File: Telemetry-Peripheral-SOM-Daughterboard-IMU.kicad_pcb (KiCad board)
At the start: 2 copper layers, 32 x 50 mm, 34 parts, among them IC1 FS3000-1015, J1 Conn_02x10_Odd_Even, J2 Conn_01x03_Pin, J3 Conn_01x03_Pin, J4 Conn_01x03_Pin, U1 LSM6DSV

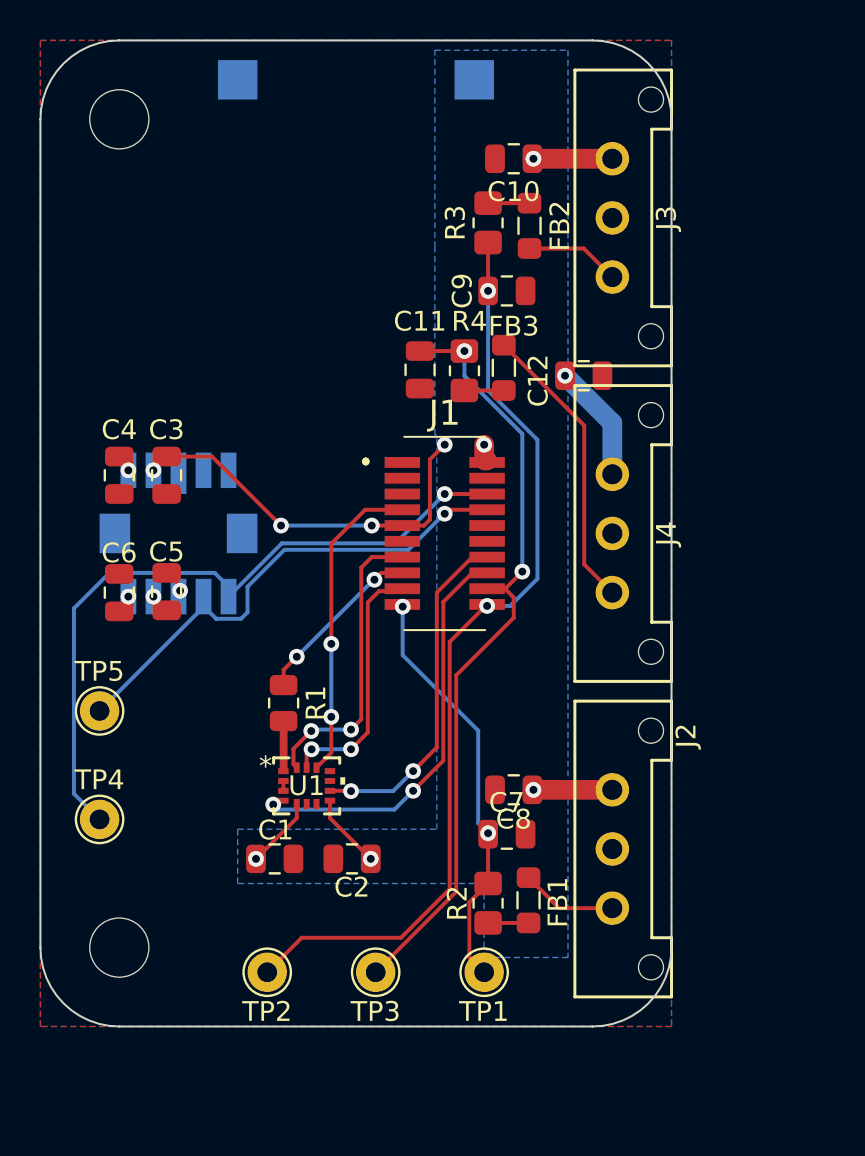
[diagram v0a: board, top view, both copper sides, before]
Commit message: Temp sensor layout changes
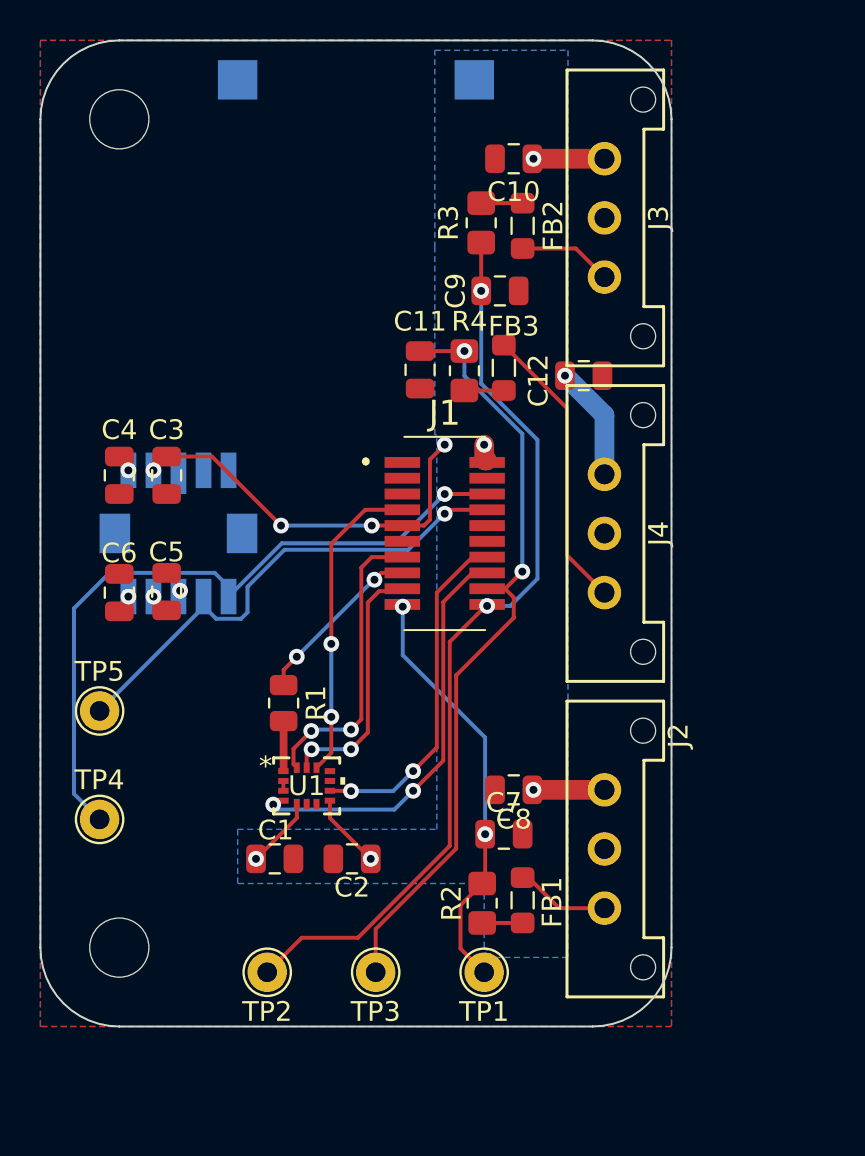
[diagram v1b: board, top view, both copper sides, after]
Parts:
- moved J2 0.40 mm to (174.6, 104.0)
- moved J3 0.40 mm to (174.6, 72.0)
- moved J4 0.40 mm to (174.6, 88.0)
- moved FB2 0.35 mm to (170.4, 75.4)
- moved C9 0.35 mm to (169.3, 78.7)
- moved R3 0.35 mm to (168.3, 75.2)
- moved FB1 0.30 mm to (170.4, 109.6)
- moved R2 0.30 mm to (168.4, 109.8)
- moved C7 0.15 mm to (169.5, 106.2)
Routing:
- net /PA1: track 47.6 -> 46.3 mm
- net +3.3V: track 42.5 -> 41.5 mm

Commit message: extended board for test points and connector
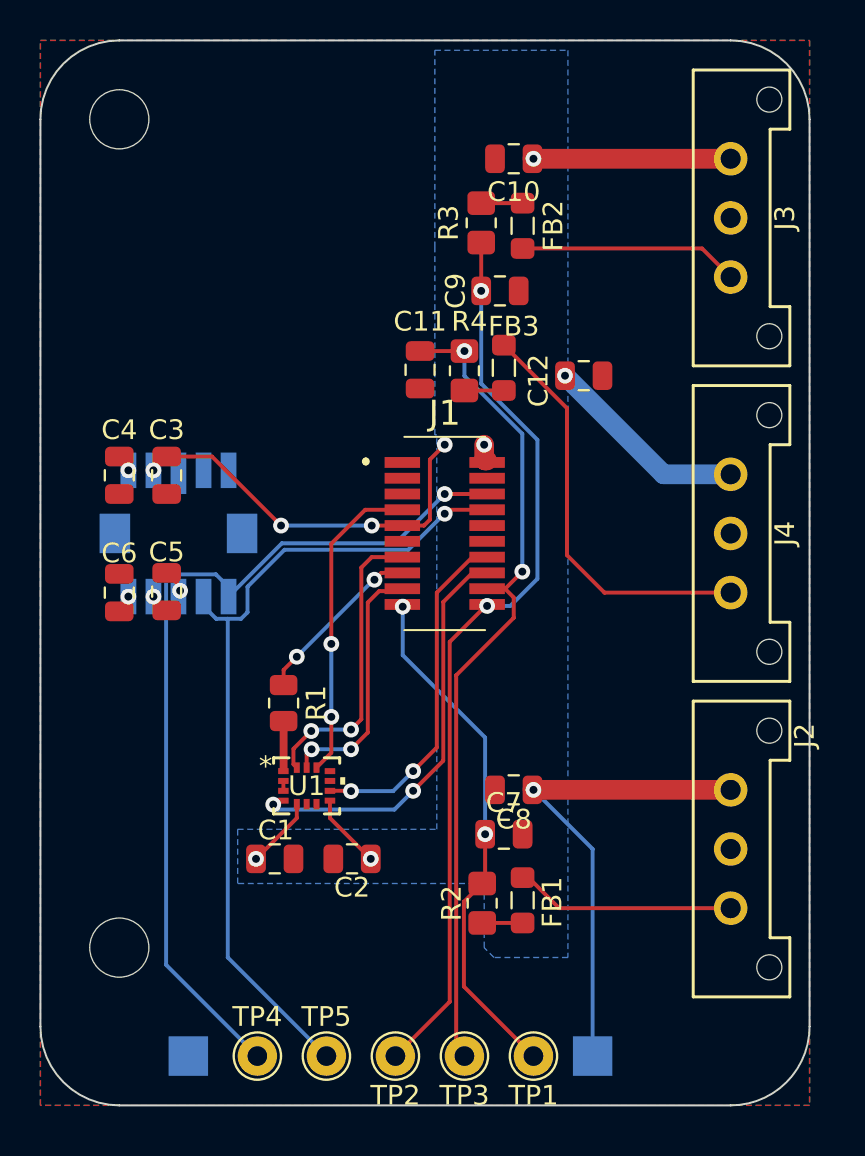
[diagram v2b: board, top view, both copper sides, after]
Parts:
- moved 3.3V_TP1 49.9 mm to (174.0, 117.5)
- moved GND_TP1 49.6 mm to (153.5, 117.5)
- moved TP5 20.9 mm to (160.5, 117.5)
- moved TP4 14.4 mm to (157.0, 117.5)
- moved TP2 7.77 mm to (164.0, 117.5)
- moved J2 6.40 mm to (181.0, 104.0)
- moved J3 6.40 mm to (181.0, 72.0)
- moved J4 6.40 mm to (181.0, 88.0)
- moved TP3 6.19 mm to (167.5, 117.5)
- moved TP1 4.93 mm to (171.0, 117.5)
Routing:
- net +3.3V: track 41.5 -> 73.7 mm
- net /I2C2_SCL: track 26.2 -> 42.4 mm
- net /I2C2_SDA: track 35.9 -> 45.5 mm
- net Net-(J4-Pin_3): track 14.7 -> 21.1 mm
- net Net-(J3-Pin_3): track 4.75 -> 11.2 mm
- net Net-(J2-Pin_3): track 4.49 -> 10.9 mm
- net /SPI1_NSS: track 21.3 -> 26.4 mm
- net /PA2: track 40.2 -> 43.0 mm
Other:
- board size 32 x 50 mm -> 39 x 54 mm

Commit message: shifted protective circuitry to be closer to connectors
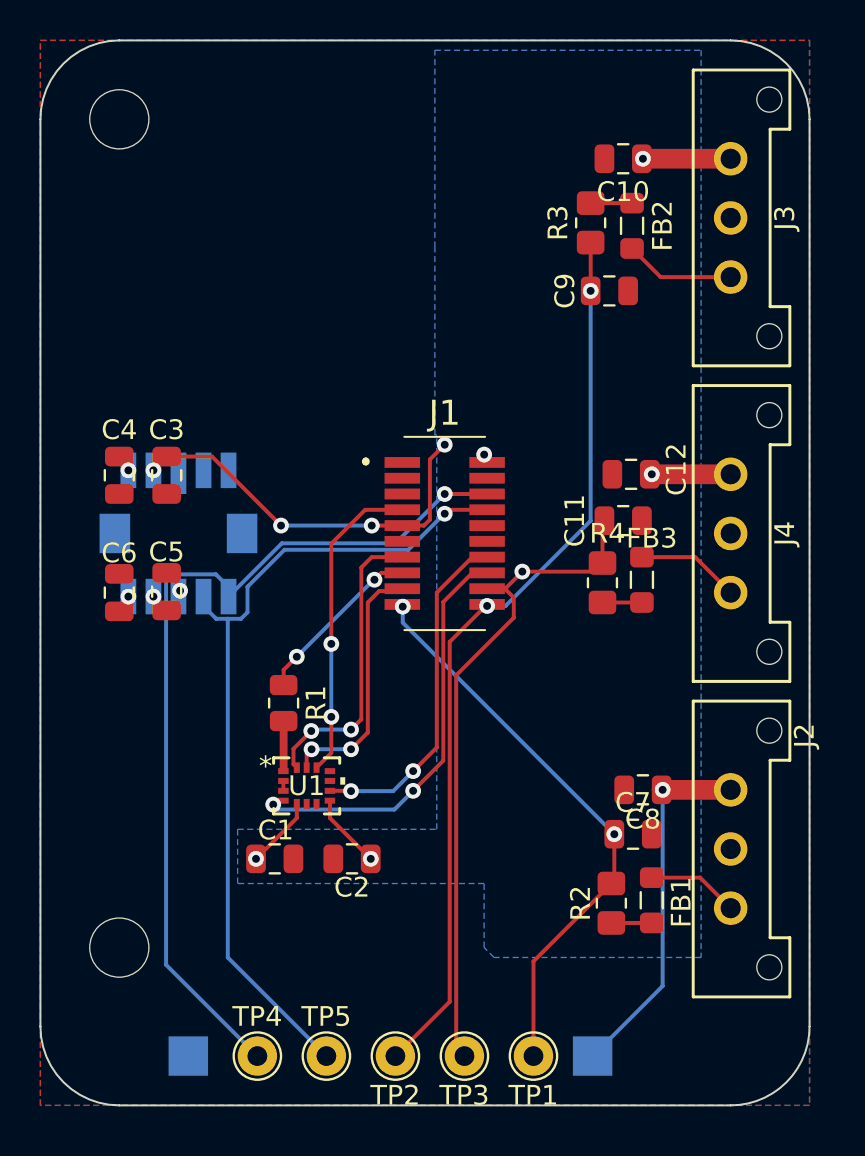
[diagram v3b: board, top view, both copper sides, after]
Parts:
- moved C11 12.8 mm to (175.6, 90.3), turned to 0 degrees
- moved FB3 12.8 mm to (176.5, 93.3)
- moved R4 12.8 mm to (174.5, 93.5)
- moved C7 6.55 mm to (176.1, 106.2)
- moved C8 6.55 mm to (176.6, 104.0)
- moved FB1 6.55 mm to (177.0, 109.6)
- moved R2 6.55 mm to (174.9, 109.8)
- moved C10 5.55 mm to (175.6, 72.0)
- moved FB2 5.55 mm to (176.0, 75.4)
- moved R3 5.55 mm to (173.9, 75.2)
- moved C9 5.55 mm to (174.8, 78.7)
- moved C12 5.55 mm to (175.9, 88.0), turned to 180 degrees
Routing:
- net +3.3V: track 73.7 -> 55.1 mm
- net Net-(J4-Pin_3): track 21.1 -> 5.25 mm
- net /PA2: track 43.0 -> 34.7 mm, vias 2 -> 1
- net Net-(J2-Pin_3): track 10.9 -> 4.64 mm
- net Net-(J3-Pin_3): track 11.2 -> 5.60 mm
- net /SPI1_NSS: track 26.4 -> 28.9 mm

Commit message: Aligning components
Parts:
- moved C7 5.90 mm to (174.9, 112.0)
- moved C11 5.78 mm to (174.9, 96.1)
- moved R3 1.45 mm to (174.0, 76.7)
- moved FB2 1.45 mm to (176.0, 76.8)
- moved R2 1.42 mm to (174.0, 108.7), turned to 90 degrees
- moved C9 1.40 mm to (174.9, 80.1)
- moved FB1 1.25 mm to (176.0, 108.8), turned to -90 degrees
- moved C8 1.00 mm to (175.6, 104.0)
- moved R4 0.94 mm to (174.0, 92.7), turned to 90 degrees
- moved FB3 0.71 mm to (176.0, 92.8), turned to -90 degrees
- moved C12 0.40 mm to (175.6, 88.0)
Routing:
- net +3.3V: track 55.1 -> 50.4 mm, vias 10 -> 9
- net /I2C2_SCL: track 42.4 -> 45.4 mm
- net /PA1: track 46.0 -> 44.0 mm, vias 2 -> 3
- net /PA2: track 34.7 -> 32.8 mm, vias 1 -> 0
- net /SPI1_NSS: track 28.9 -> 30.3 mm
- net /I2C2_SDA: track 45.5 -> 46.2 mm
- net Net-(J3-Pin_3): track 5.60 -> 5.00 mm
- net /SPI2_NSS: vias 2 -> 0

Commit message: Finalizing board layout changes
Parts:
- 3.3V_TP1, GND_TP1: moved to F.Cu
- turned 3.3V_TP1 to 0 degrees
- turned GND_TP1 to 0 degrees
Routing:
- net /I2C2_SCL: track 45.4 -> 44.9 mm, vias 1 -> 3
- net +3.3V: track 50.4 -> 50.6 mm, vias 9 -> 10
- net /I2C2_SDA: vias 1 -> 3
- net GND: vias 0 -> 23
- net /PA1: vias 3 -> 2
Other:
- board text added: "Telemetry Peripheral SOM Daughterboard Fall 2023 - Design by Andrew Nguyen, Frank Li, Jim Fang"
- board text removed: "Telemetry Peripheral SOM Daughterboard IMU Fall 2023 - Design by Andrew Nguyen, Frank Li, Jim Fang"

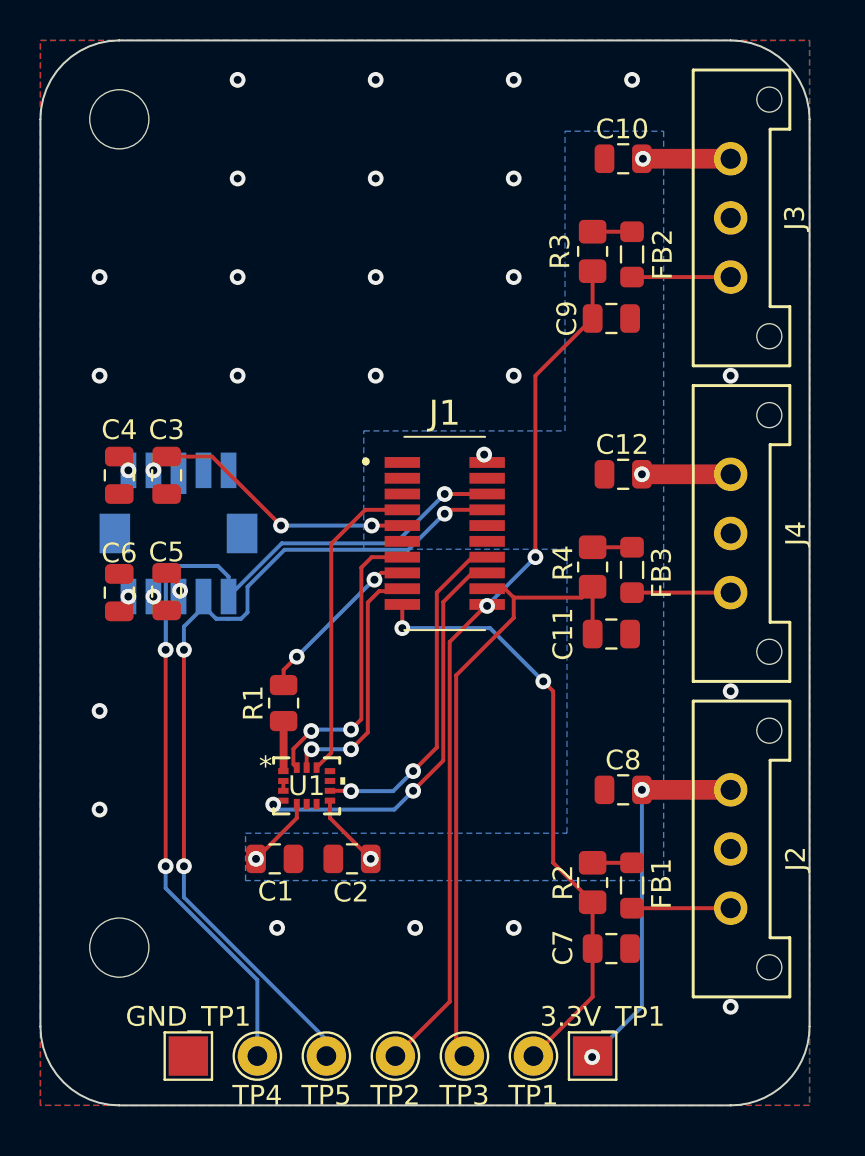
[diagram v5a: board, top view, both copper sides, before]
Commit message: Changes to routing and silkscreen, addressed schematic error
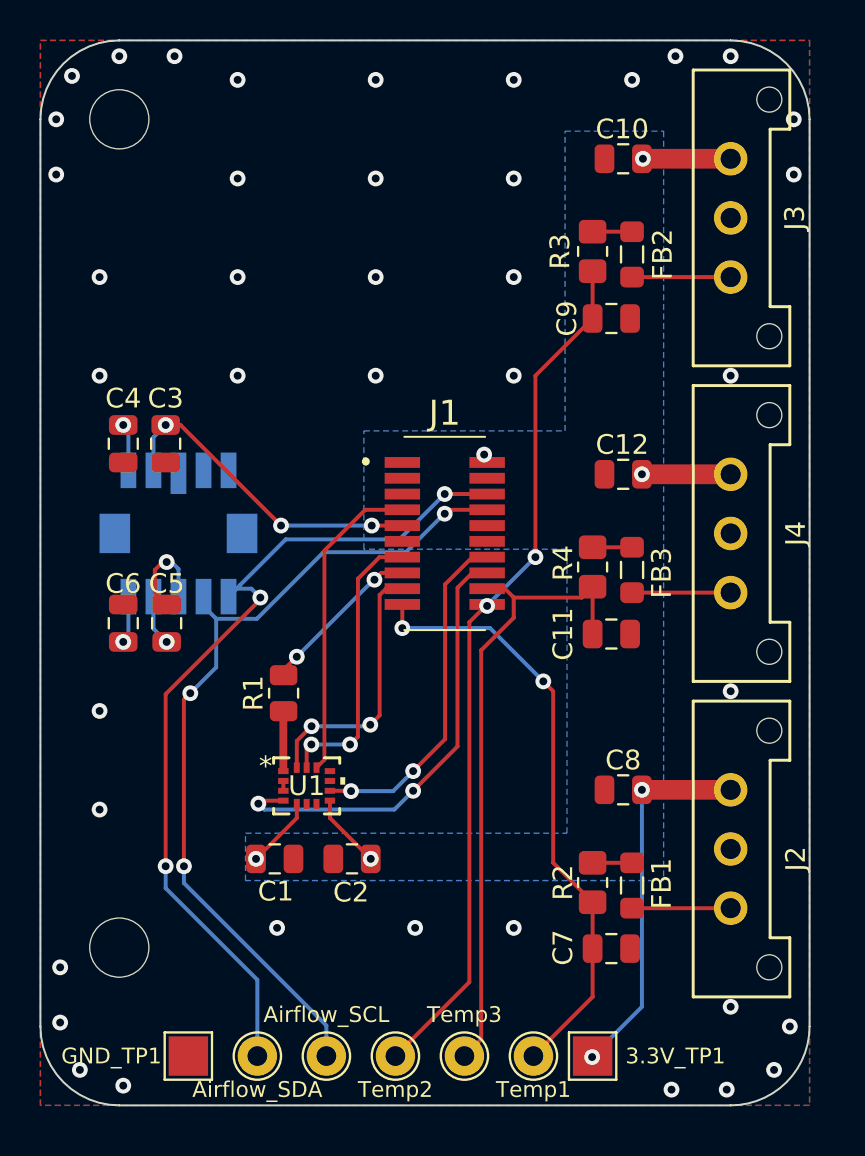
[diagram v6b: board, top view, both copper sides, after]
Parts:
- moved C4 1.61 mm to (150.2, 86.5)
- moved C3 1.60 mm to (152.3, 86.5)
- moved C5 1.60 mm to (152.4, 95.5)
- moved C6 1.56 mm to (150.2, 95.5)
- moved R1 0.50 mm to (158.3, 99.1)
- renumbered TP5 to Airflow_SCL, TP4 to Airflow_SDA, TP1 to Temp1, TP2 to Temp2, TP3 to Temp3
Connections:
- U1 pad 13: /SPI1_MOSI -> /SPI1_SCK
- U1 pad 14: /SPI1_SCK -> /SPI1_MOSI
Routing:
- net Net-(IC1-TP1): track 1.18 -> 4.91 mm
- net +3.3V: track 50.6 -> 52.9 mm
- net /I2C2_SDA: track 46.2 -> 44.4 mm
- net /I2C2_SCL: track 44.9 -> 43.3 mm
- net Net-(IC1-TP2): track 0.98 -> 2.58 mm
- net Net-(IC1-VREG): track 0.89 -> 2.41 mm
- net /I2C1_SDA: track 21.2 -> 22.7 mm
- net Net-(IC1-VCM): track 0.94 -> 2.41 mm
- net Net-(U1-SDO/SA0): track 2.50 -> 3.19 mm
- net /SPI1_MOSI: track 12.9 -> 13.5 mm
- net /SPI1_SCK: track 15.1 -> 14.5 mm
- net /SPI1_MISO: track 8.82 -> 8.32 mm
- net GND: track 0.52 -> 0.50 mm, vias 23 -> 40
